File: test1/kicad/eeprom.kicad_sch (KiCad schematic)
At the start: 4 parts, among them U1 24AA08

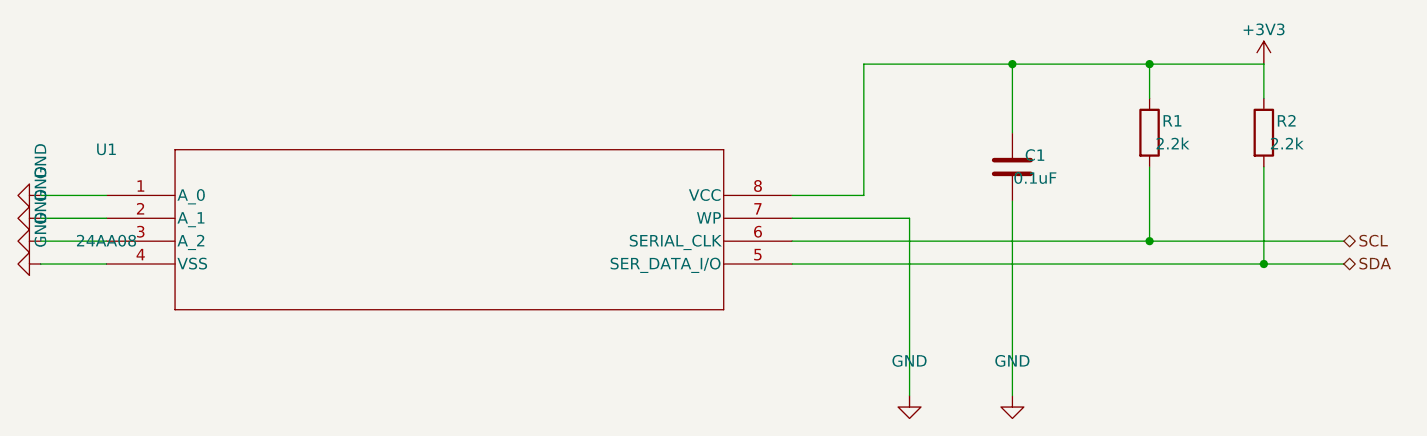
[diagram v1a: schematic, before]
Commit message: Project-wide connectivity audit: refdes uniqueness + hier-label correctness
Added test1/verify_project.py as a kicad-cli-erc substitute (the dev
build doesn't ship _cvpcb.kiface, so sch erc is broken). The verifier
parses all .kicad_sch files and checks:
  1. Duplicate refdes (KiCad's refdes namespace is project-wide).
  2. Parent sheet-pin name + direction matches child hierarchical_label.
  3. Orphan child hierarchical_labels (no matching parent pin).

First run flagged 48 issues. Now reports 0.

Refdes scheme — per-sheet decade ranges so global namespace stays unique:
  FMC 1-9 (J1-J4)
  Power 10-19 (U10/U11, R10/R11, C10-C16, J10-J12)
  Bobcat 20-29 (U20, R20/R21, C20-C25)
  EEPROM 30-39 (U30, R30/R31, C30)
  Bias 40-49 (U40/U41 [U41 dual-unit OPA], Q40-Q43, R40/R41, C40-C43)
  Connectors 50-59 (J50-J57, TP50-TP52)

Hierarchical / global label rework:
  - Parent sheet-pin directions corrected to match child labels (was
    flipped on every Bobcat SPI pin and on FMC's LDO_EN/LSW_EN/LDO_PG).
  - Bobcat SPI labels: passive → input/output as appropriate.
  - Project-wide nets converted to global_label (auto-tie by name, no
    parent pins): SCL, SDA, SAMPLE_OUT*, OSC_EN, WEIGHT_EN, SAMPLE_TRIG,
    BIAS_ISO0/1, CS_L, SCLK, MOSI, MISO, SPI_DMODE, RESET_N.
  - hier_label retained for clean 2-sheet pairs: VADJ, LDO_EN, LDO_PG,
    LSW_EN (FMC ↔ Power); BIAS0/1 (Bias ↔ Bobcat); CLK_OUT0-3, GPIO0-3
    (Bobcat ↔ Connectors).
  - Visual cue in renders: globals render as boxed rectangles; hierarchical
    labels render as arrows — handy when scanning a sheet.

Memory: appended five connectivity-correctness lessons to
feedback_kicad_generator_lessons.md (refdes namespace, parent/child
direction parity, no-passive-for-real-signals, global vs hier decision
table, verify-after-every-change).

Co-Authored-By: Claude Opus 4.7 (1M context) <noreply@anthropic.com>
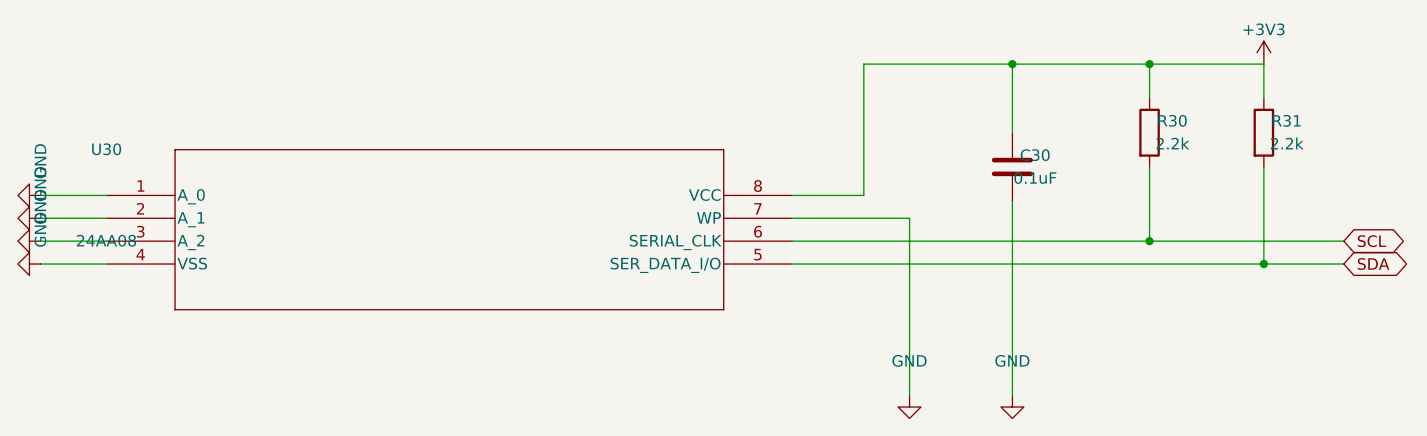
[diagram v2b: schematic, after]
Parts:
- removed C1: 0.1uF, Capacitor_SMD:C_0402_1005Metric, symbol Device:C
- removed R1, R2: 2.2k, Resistor_SMD:R_0402_1005Metric, symbol Device:R
- removed U1: 24AA08, Package_SO:SOIC-8_3.9x4.9mm_P1.27mm, symbol Lib:24AA08-I-SN
- added C30: 0.1uF, Capacitor_SMD:C_0402_1005Metric, symbol Device:C
- added R30, R31: 2.2k, Resistor_SMD:R_0402_1005Metric, symbol Device:R
- added U30: 24AA08, Package_SO:SOIC-8_3.9x4.9mm_P1.27mm, symbol Lib:24AA08-I-SN
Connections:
- net +3V3: now also C30.1, R30.1, R31.1, U30.8 (VCC)
- net GND: now also C30.2, U30.1 (A_0), U30.2 (A_1), U30.3 (A_2), U30.4 (VSS), U30.7 (WP)
- net SCL: now also R30.2, U30.6 (SERIAL_CLK)
- net SDA: now also R31.2, U30.5 (SER_DATA_I/O)
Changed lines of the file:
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@@
     (at 100 120 0)
     (unit 1) (in_bom yes) (on_board yes) (dnp no)
-    (property "Reference" "U1" (at 100 114.92 0) (effects (font (size 1.27 1.27))))
+    (property "Reference" "U30" (at 100 114.92 0) (effects (font (size 1.27 1.27))))
     (property "Value" "24AA08" (at 100 125.08 0) (effects (font (size 1.27 1.27))))
     (property "Footprint" "Package_SO:SOIC-8_3.9x4.9mm_P1.27mm" (at 0 0 0) (effects (font (size 1.27 1.27)) (hide yes)))
@@
     (instances
       (project "test1"
-        (path "/4ed7a046-ef33-57d9-8730-321c05965af3/14a26295-3b60-56cd-8552-ba2c699fffdc" (reference "U1") (unit 1)))))
+        (path "/4ed7a046-ef33-57d9-8730-321c05965af3/14a26295-3b60-56cd-8552-ba2c699fffdc" (reference "U30") (unit 1)))))
   (wire (pts (xy 100 120) (xy 92.71 120)) (stroke (width 0) (type default)))
   (symbol
@@
         (path "/4ed7a046-ef33-57d9-8730-321c05965af3/14a26295-3b60-56cd-8552-ba2c699fffdc" (reference "#PWR5e47453c") (unit 1)))))
   (wire (pts (xy 176.2 125.08) (xy 237.49 125.08)) (stroke (width 0) (type default)))
-  (hierarchical_label "SCL" (shape bidirectional) (at 237.49 125.08 0) (effects (font (size 1.27 1.27)) (justify left)))
+  (global_label "SCL" (shape bidirectional) (at 237.49 125.08 0) (effects (font (size 1.27 1.27)) (justify left)))
   (wire (pts (xy 176.2 127.62) (xy 237.49 127.62)) (stroke (width 0) (type default)))
-  (hierarchical_label "SDA" (shape bidirectional) (at 237.49 127.62 0) (effects (font (size 1.27 1.27)) (justify left)))
+  (global_label "SDA" (shape bidirectional) (at 237.49 127.62 0) (effects (font (size 1.27 1.27)) (justify left)))
   (symbol
     (lib_id "Device:C")
     (at 200.66 116.84 0)
     (unit 1) (in_bom yes) (on_board yes) (dnp no)
-    (property "Reference" "C1" (at 203.2 115.57000000000001 0) (effects (font (size 1.27 1.27))))
+    (property "Reference" "C30" (at 203.2 115.57000000000001 0) (effects (font (size 1.27 1.27))))
     (property "Value" "0.1uF" (at 203.2 118.11 0) (effects (font (size 1.27 1.27))))
     (property "Footprint" "Capacitor_SMD:C_0402_1005Metric" (at 0 0 0) (effects (font (size 1.27 1.27)) (hide yes)))
@@
     (instances
       (project "test1"
-        (path "/4ed7a046-ef33-57d9-8730-321c05965af3/14a26295-3b60-56cd-8552-ba2c699fffdc" (reference "C1") (unit 1)))))
+        (path "/4ed7a046-ef33-57d9-8730-321c05965af3/14a26295-3b60-56cd-8552-ba2c699fffdc" (reference "C30") (unit 1)))))
   (wire (pts (xy 200.66 113.03) (xy 200.66 105.41)) (stroke (width 0) (type default)))
   (wire (pts (xy 200.66 120.65) (xy 200.66 142.24)) (stroke (width 0) (type default)))
@@
     (at 215.9 113.03 0)
     (unit 1) (in_bom yes) (on_board yes) (dnp no)
-    (property "Reference" "R1" (at 218.44 111.76 0) (effects (font (size 1.27 1.27))))
+    (property "Reference" "R30" (at 218.44 111.76 0) (effects (font (size 1.27 1.27))))
     (property "Value" "2.2k" (at 218.44 114.3 0) (effects (font (size 1.27 1.27))))
     (property "Footprint" "Resistor_SMD:R_0402_1005Metric" (at 0 0 0) (effects (font (size 1.27 1.27)) (hide yes)))
@@
     (instances
       (project "test1"
-        (path "/4ed7a046-ef33-57d9-8730-321c05965af3/14a26295-3b60-56cd-8552-ba2c699fffdc" (reference "R1") (unit 1)))))
+        (path "/4ed7a046-ef33-57d9-8730-321c05965af3/14a26295-3b60-56cd-8552-ba2c699fffdc" (reference "R30") (unit 1)))))
   (wire (pts (xy 215.9 109.22) (xy 215.9 105.41)) (stroke (width 0) (type default)))
   (wire (pts (xy 215.9 116.84) (xy 215.9 125.08)) (stroke (width 0) (type default)))
@@
     (at 228.6 113.03 0)
     (unit 1) (in_bom yes) (on_board yes) (dnp no)
-    (property "Reference" "R2" (at 231.14 111.76 0) (effects (font (size 1.27 1.27))))
+    (property "Reference" "R31" (at 231.14 111.76 0) (effects (font (size 1.27 1.27))))
     (property "Value" "2.2k" (at 231.14 114.3 0) (effects (font (size 1.27 1.27))))
     (property "Footprint" "Resistor_SMD:R_0402_1005Metric" (at 0 0 0) (effects (font (size 1.27 1.27)) (hide yes)))
@@
     (instances
       (project "test1"
-        (path "/4ed7a046-ef33-57d9-8730-321c05965af3/14a26295-3b60-56cd-8552-ba2c699fffdc" (reference "R2") (unit 1)))))
+        (path "/4ed7a046-ef33-57d9-8730-321c05965af3/14a26295-3b60-56cd-8552-ba2c699fffdc" (reference "R31") (unit 1)))))
   (wire (pts (xy 228.6 109.22) (xy 228.6 105.41)) (stroke (width 0) (type default)))
   (wire (pts (xy 228.6 116.84) (xy 228.6 127.62)) (stroke (width 0) (type default)))

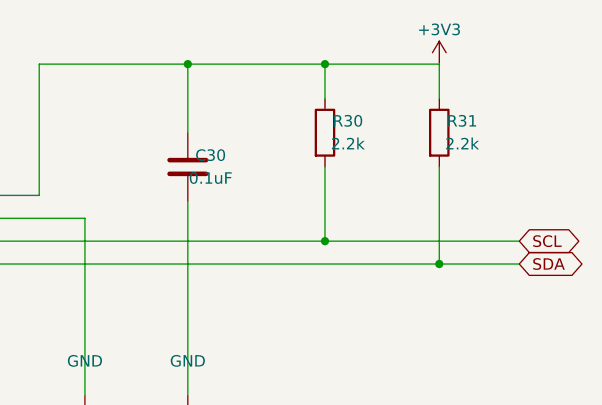
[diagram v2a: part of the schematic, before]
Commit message: Split test1 generator into per-sheet package with netlist YAML + strict validator
Combines three layered changes:

1. Apply the design-review audit (test1/error_log.md): 9 ERRORs + 10
   WARNINGs from the new .claude/skills/design_review.md skill — FMC
   LA-bank 0Ω routing, Bobcat SPI/control/GPIO pull network, LDO
   ANY-OUT to FPGA, LDO_PG pull-up + series, bias DNP convention,
   kelvin SNS, per-pin VDDIO + bulk caps, BIAS bypass, VADJ/VDDIO bulk,
   MCP4728 EEPROM provisioning notes, shared-rail decision documented.

2. Refactor test1/gen_schematic.py (1825 lines → 138-line entry point)
   into a per-sheet package at test1/gen/:
     config.py / symbols.py / shared.py  — primitives, Sheet container,
     LA_ASSIGN, footprints, sexpr emit
     build_<sheet>.py × 7                — one builder per child sheet
     netlist.py / validator.py           — YAML loader + strict checker
   Per-session context for any single sheet drops to ~500 lines.
   Also sorts non-deterministic set iteration that made fmc.kicad_sch
   diff noisily across runs.

3. Add a declarative connectivity layer (netlist/<sheet>.yaml):
   parts inventory + nets (power / hier / global / internal), with
   explicit unit syntax for multi-unit symbols (U41:u2.7, J3:u3.G16).
   The strict validator runs at the end of every build_<sheet>() call:
     - inventory: YAML parts ↔ placed (refdes, unit) parity
     - connectivity: every YAML net member is in a connected component
       named the YAML net name (Union-Find on wires + junctions + label
       anchors + power-symbol pins; T-intersections auto-connect)
     - internal nets: members in one component, no name check
   Sheet now records structured PlacedPart/wire/label data alongside
   the s-expr emit; validator reads those instead of re-parsing.

All 6 child sheets' .kicad_sch outputs are byte-identical to the
post-design-review reference, and verify_project.py reports 0 issues.

Co-Authored-By: Claude Opus 4.7 (1M context) <noreply@anthropic.c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
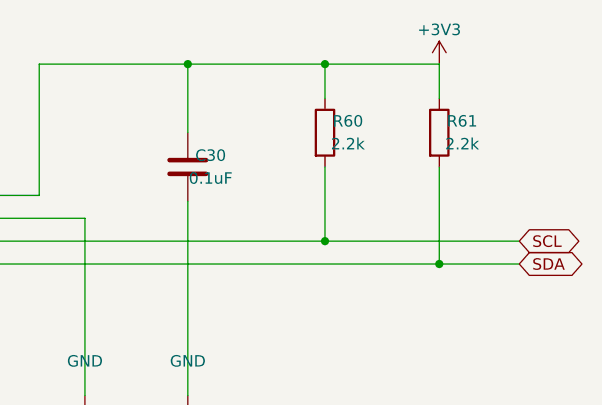
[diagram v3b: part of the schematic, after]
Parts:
- removed R30, R31: 2.2k, Resistor_SMD:R_0402_1005Metric, symbol Device:R
- added R60, R61: 2.2k, Resistor_SMD:R_0402_1005Metric, symbol Device:R
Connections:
- net +3V3: now also R60.1, R61.1
- net SCL: now also R60.2
- net SDA: now also R61.2
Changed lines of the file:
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@@
     (at 215.9 113.03 0)
     (unit 1) (in_bom yes) (on_board yes) (dnp no)
-    (property "Reference" "R30" (at 218.44 111.76 0) (effects (font (size 1.27 1.27))))
+    (property "Reference" "R60" (at 218.44 111.76 0) (effects (font (size 1.27 1.27))))
     (property "Value" "2.2k" (at 218.44 114.3 0) (effects (font (size 1.27 1.27))))
     (property "Footprint" "Resistor_SMD:R_0402_1005Metric" (at 0 0 0) (effects (font (size 1.27 1.27)) (hide yes)))
@@
     (instances
       (project "test1"
-        (path "/4ed7a046-ef33-57d9-8730-321c05965af3/14a26295-3b60-56cd-8552-ba2c699fffdc" (reference "R30") (unit 1)))))
+        (path "/4ed7a046-ef33-57d9-8730-321c05965af3/14a26295-3b60-56cd-8552-ba2c699fffdc" (reference "R60") (unit 1)))))
   (wire (pts (xy 215.9 109.22) (xy 215.9 105.41)) (stroke (width 0) (type default)))
   (wire (pts (xy 215.9 116.84) (xy 215.9 125.08)) (stroke (width 0) (type default)))
@@
     (at 228.6 113.03 0)
     (unit 1) (in_bom yes) (on_board yes) (dnp no)
-    (property "Reference" "R31" (at 231.14 111.76 0) (effects (font (size 1.27 1.27))))
+    (property "Reference" "R61" (at 231.14 111.76 0) (effects (font (size 1.27 1.27))))
     (property "Value" "2.2k" (at 231.14 114.3 0) (effects (font (size 1.27 1.27))))
     (property "Footprint" "Resistor_SMD:R_0402_1005Metric" (at 0 0 0) (effects (font (size 1.27 1.27)) (hide yes)))
@@
     (instances
       (project "test1"
-        (path "/4ed7a046-ef33-57d9-8730-321c05965af3/14a26295-3b60-56cd-8552-ba2c699fffdc" (reference "R31") (unit 1)))))
+        (path "/4ed7a046-ef33-57d9-8730-321c05965af3/14a26295-3b60-56cd-8552-ba2c699fffdc" (reference "R61") (unit 1)))))
   (wire (pts (xy 228.6 109.22) (xy 228.6 105.41)) (stroke (width 0) (type default)))
   (wire (pts (xy 228.6 116.84) (xy 228.6 127.62)) (stroke (width 0) (type default)))

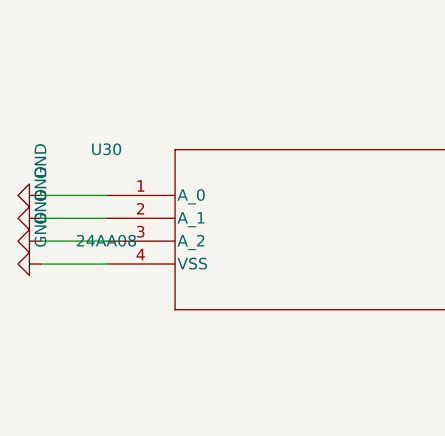
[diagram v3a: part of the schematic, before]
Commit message: Add layout linter + cluster helpers; fix silent shorts across sheets
Introduces gen/layout_lint.py with checks for bbox spacing, wires
through/into a body, parallel-wire overlap on the same axis, bridged
drop columns, and dense GND clusters — non-fatal warnings the strict
validator cannot catch (each net's name is still present in a bridged
component's name set, so per-member name checks pass).

Fixes the bugs the linter exposed:
- FMC routing flipped to exit LEFT (pin-protrusion side) so wires no
  longer pass through the connector body
- bobcat OWT (pins 23-25) + GPIO (37-40) get one drop column per pin,
  ending the silent shorts between adjacent nets
- bobcat SPI pin 14 pull-x shifted off pin 19's column
- bias Q40/Q41 source/drain wires detoured around the body so source
  no longer shorts to drain through the same vertical
- power LDO redundant tap stubs + GND-rail dupes removed; C12 moved
  off R10's column so NR_SS doesn't short to GND
- C11 ↔ R10, J54-56 ↔ R50-52 spacing widened to meet bbox rule

Adds gnd_bus() and decoupling_cluster() helpers in gen/shared.py and
applies gnd_bus() to the eeprom address-strap pins.

Skill doc gets rules for pin-protrusion side, per-pin drop columns,
and same-axis wire overlap. All 7 sheets now pass kicad-cli parse,
the strict connectivity validator, and the layout linter.

Co-Authored-By: Claude Opus 4.7 (1M context) <noreply@anthropic.com>
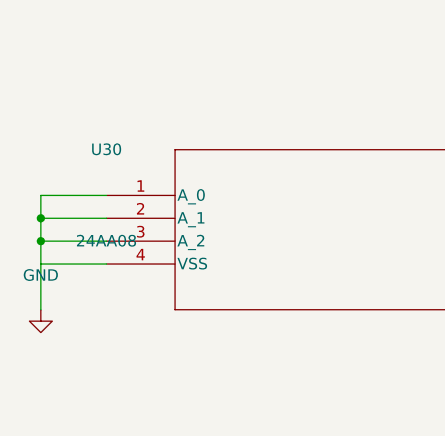
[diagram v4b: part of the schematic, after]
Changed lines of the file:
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@@
         (path "/4ed7a046-ef33-57d9-8730-321c05965af3/14a26295-3b60-56cd-8552-ba2c699fffdc" (reference "U30") (unit 1)))))
   (wire (pts (xy 100 120) (xy 92.71 120)) (stroke (width 0) (type default)))
+  (wire (pts (xy 100 122.54) (xy 92.71 122.54)) (stroke (width 0) (type default)))
+  (wire (pts (xy 100 125.08) (xy 92.71 125.08)) (stroke (width 0) (type default)))
+  (wire (pts (xy 100 127.62) (xy 92.71 127.62)) (stroke (width 0) (type default)))
+  (wire (pts (xy 92.71 120) (xy 92.71 127.62)) (stroke (width 0) (type default)))
+  (junction (at 92.71 122.54) (diameter 0) (color 0 0 0 0))
+  (junction (at 92.71 125.08) (diameter 0) (color 0 0 0 0))
+  (wire (pts (xy 92.71 127.62) (xy 92.71 132.70000000000002)) (stroke (width 0) (type default)))
   (symbol
     (lib_id "power:GND")
-    (at 92.71 120 270)
+    (at 92.71 132.70000000000002 0)
     (unit 1) (in_bom yes) (on_board yes) (dnp no)
-    (property "Reference" "#PWR90b2b870" (at 92.71 113.65 0) (effects (font (size 1.27 1.27)) (hide yes)))
-    (property "Value" "GND" (at 92.71 116.19 0) (effects (font (size 1.27 1.27))))
+    (property "Reference" "#PWReb3a2c9f" (at 92.71 126.35000000000002 0) (effects (font (size 1.27 1.27)) (hide yes)))
+    (property "Value" "GND" (at 92.71 128.89000000000001 0) (effects (font (size 1.27 1.27))))
     (property "Footprint" "" (at 0 0 0) (effects (font (size 1.27 1.27)) (hide yes)))
     (property "Datasheet" "" (at 0 0 0) (effects (font (size 1.27 1.27)) (hide yes)))
@@
     (instances
       (project "test1"
-        (path "/4ed7a046-ef33-57d9-8730-321c05965af3/14a26295-3b60-56cd-8552-ba2c699fffdc" (reference "#PWR90b2b870") (unit 1)))))
-  (wire (pts (xy 100 122.54) (xy 92.71 122.54)) (stroke (width 0) (type default)))
-  (symbol
-    (lib_id "power:GND")
-    (at 92.71 122.54 270)
-    (unit 1) (in_bom yes) (on_board yes) (dnp no)
-    (property "Reference" "#PWR1ec9cb95" (at 92.71 116.19000000000001 0) (effects (font (size 1.27 1.27)) (hide yes)))
-    (property "Value" "GND" (at 92.71 118.73 0) (effects (font (size 1.27 1.27))))
-    (property "Footprint" "" (at 0 0 0) (effects (font (size 1.27 1.27)) (hide yes)))
-    (property "Datasheet" "" (at 0 0 0) (effects (font (size 1.27 1.27)) (hide yes)))
-    (pin "1")
-    (instances
-      (project "test1"
-        (path "/4ed7a046-ef33-57d9-8730-321c05965af3/14a26295-3b60-56cd-8552-ba2c699fffdc" (reference "#PWR1ec9cb95") (unit 1)))))
-  (wire (pts (xy 100 125.08) (xy 92.71 125.08)) (stroke (width 0) (type default)))
-  (symbol
-    (lib_id "power:GND")
-    (at 92.71 125.08 270)
-    (unit 1) (in_bom yes) (on_board yes) (dnp no)
-    (property "Reference" "#PWRc474bad9" (at 92.71 118.73 0) (effects (font (size 1.27 1.27)) (hide yes)))
-    (property "Value" "GND" (at 92.71 121.27 0) (effects (font (size 1.27 1.27))))
-    (property "Footprint" "" (at 0 0 0) (effects (font (size 1.27 1.27)) (hide yes)))
-    (property "Datasheet" "" (at 0 0 0) (effects (font (size 1.27 1.27)) (hide yes)))
-    (pin "1")
-    (instances
-      (project "test1"
-        (path "/4ed7a046-ef33-57d9-8730-321c05965af3/14a26295-3b60-56cd-8552-ba2c699fffdc" (reference "#PWRc474bad9") (unit 1)))))
-  (wire (pts (xy 100 127.62) (xy 92.71 127.62)) (stroke (width 0) (type default)))
-  (symbol
-    (lib_id "power:GND")
-    (at 92.71 127.62 270)
-    (unit 1) (in_bom yes) (on_board yes) (dnp no)
-    (property "Reference" "#PWR03cd7f12" (at 92.71 121.27000000000001 0) (effects (font (size 1.27 1.27)) (hide yes)))
-    (property "Value" "GND" (at 92.71 123.81 0) (effects (font (size 1.27 1.27))))
-    (property "Footprint" "" (at 0 0 0) (effects (font (size 1.27 1.27)) (hide yes)))
-    (property "Datasheet" "" (at 0 0 0) (effects (font (size 1.27 1.27)) (hide yes)))
-    (pin "1")
-    (instances
-      (project "test1"
-        (path "/4ed7a046-ef33-57d9-8730-321c05965af3/14a26295-3b60-56cd-8552-ba2c699fffdc" (reference "#PWR03cd7f12") (unit 1)))))
+        (path "/4ed7a046-ef33-57d9-8730-321c05965af3/14a26295-3b60-56cd-8552-ba2c699fffdc" (reference "#PWReb3a2c9f") (unit 1)))))
   (wire (pts (xy 176.2 120) (xy 184.15 120)) (stroke (width 0) (type default)))
   (wire (pts (xy 184.15 120) (xy 184.15 105.41)) (stroke (width 0) (type default)))
